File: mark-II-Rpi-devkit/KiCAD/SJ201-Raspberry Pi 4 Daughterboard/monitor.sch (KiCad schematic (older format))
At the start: 0 parts

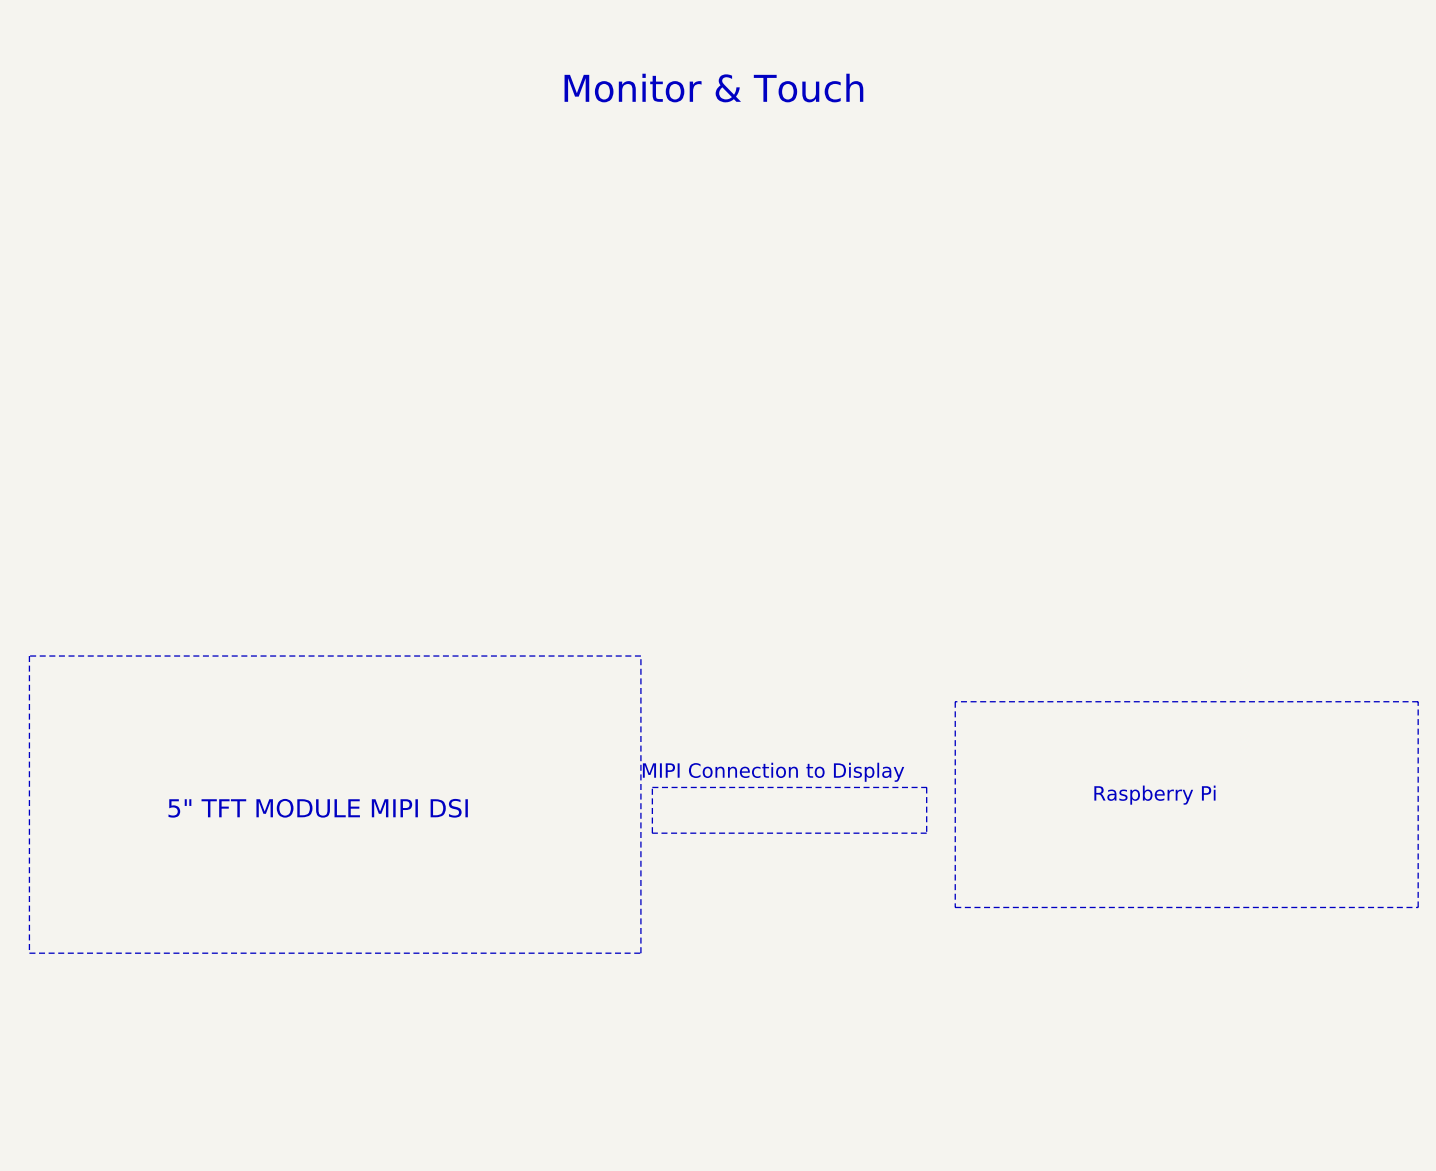
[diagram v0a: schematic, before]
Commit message: Rev4 Update - fix some wiring, export for printing Rev 4
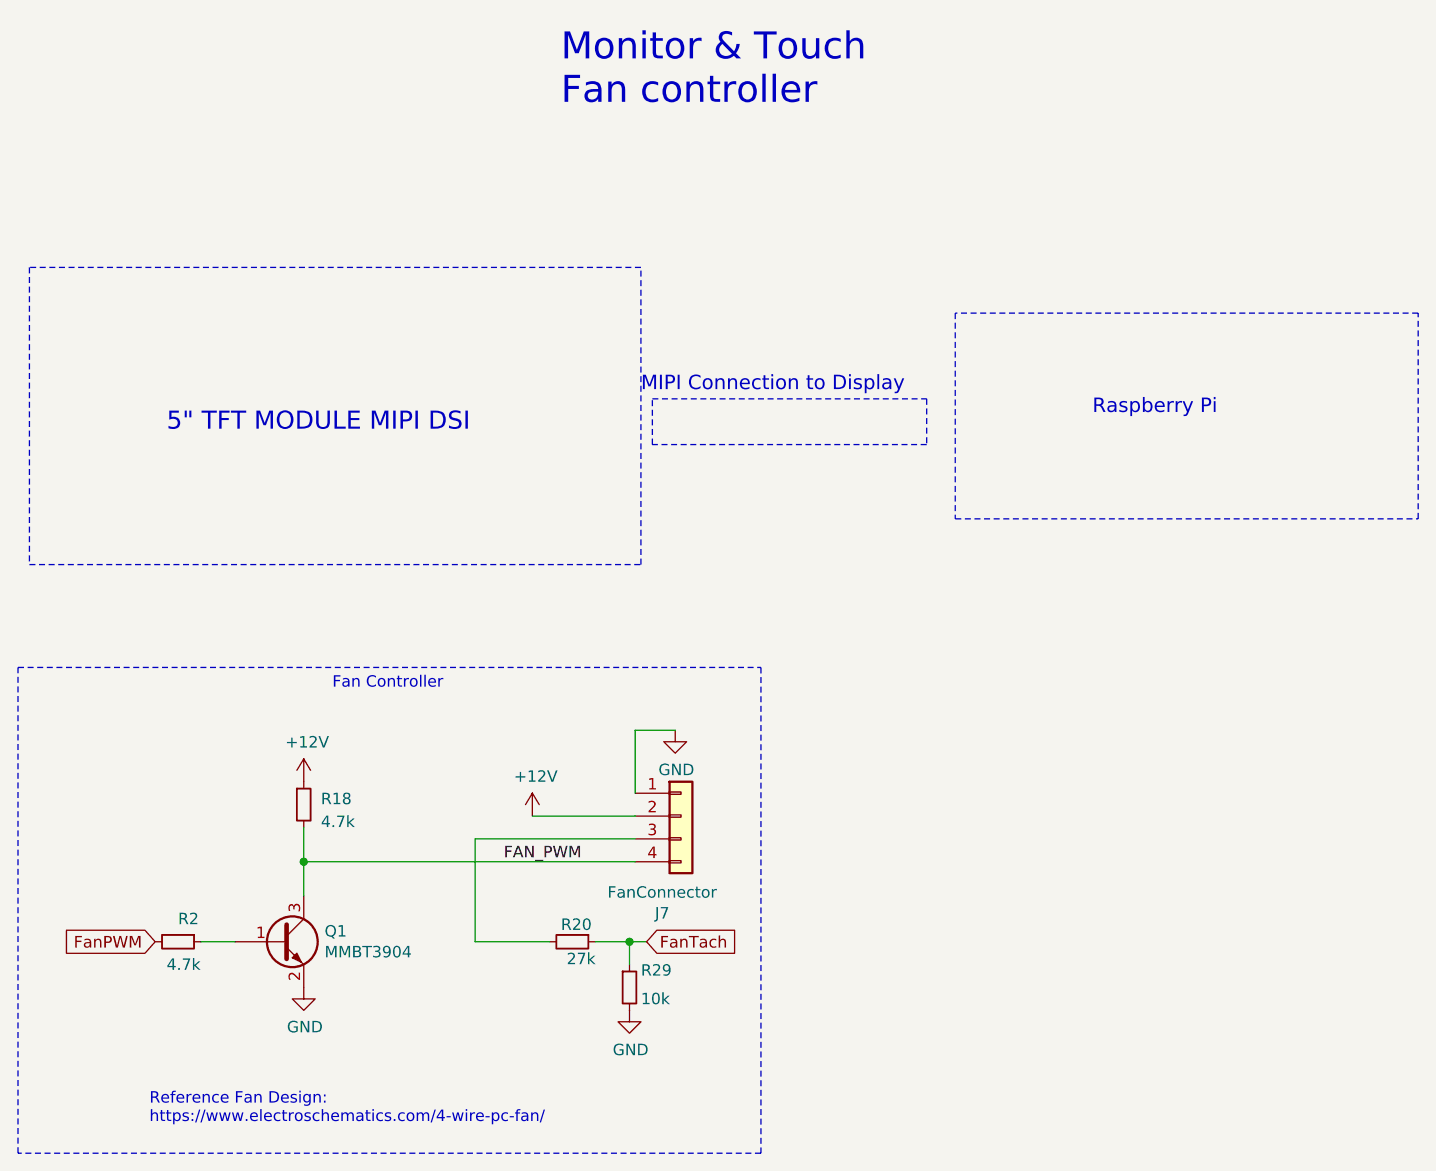
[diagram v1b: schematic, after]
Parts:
- added J7: FanConnector, Connector:FanPinHeader_1x04_P2.54mm_Vertical, symbol Connector_Generic:Conn_01x04
- added Q1: MMBT3904, Package_TO_SOT_SMD:SOT-23, symbol Transistor_BJT:MMBT3904
- added R18, R2: 4.7k, Resistor_SMD:R_0402_1005Metric, symbol Device:R_Small
- added R20: 27k, Resistor_SMD:R_0402_1005Metric, symbol Device:R_Small
- added R29: 10k, Resistor_SMD:R_0402_1005Metric, symbol Device:R_Small
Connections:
- new net: Q1.1 (B), R2.1
- new net: J7.3 (Pin_3), R20.2
- new net +12V: J7.2 (Pin_2), R18.1
- new net FAN_PWM: J7.4 (Pin_4), Q1.3 (C), R18.2
- new net FanPWM: R2.2
- new net FanTach: R20.1, R29.1
- new net GND: J7.1 (Pin_1), Q1.2 (E), R29.2
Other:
- note added: "Fan Controller"
- note added: "Monitor & Touch\nFan controller"
- note added: "Reference Fan Design:\nhttps://www.electroschematics.com/4-wire-pc-fan/"
- note removed: "Monitor & Touch"
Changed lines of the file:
@@
 Sheet 4 7
 Title ""
-Date "2020-11-18"
-Rev "rev4 - 0.01"
+Date "2020-11-22"
+Rev "Rev4 - 0.03"
 Comp "Mycroft"
-Comment1 "SJ201 r4.01"
+Comment1 "SJ-201-R4"
 Comment2 ""
 Comment3 ""
@@
 $EndDescr
 Text Notes 4725 875  0    118  ~ 0
-Monitor & Touch
-Text Notes 7050 3925 0    63   ~ 0
+Monitor & Touch\nFan controller
+Text Notes 7050 2225 0    63   ~ 0
 Raspberry Pi
-Text Notes 5075 3825 0    63   ~ 0
+Text Notes 5075 2125 0    63   ~ 0
 MIPI Connection to Display
 Wire Notes Line
-	5125 4050 5125 3850
-Wire Notes Line
-	6325 4050 5125 4050
-Wire Notes Line
-	6325 3850 6325 4050
-Wire Notes Line
-	5125 3850 6325 3850
-Wire Notes Line
-	8475 3475 6450 3475
-Wire Notes Line
-	8475 4375 8475 3475
-Wire Notes Line
-	6450 4375 8475 4375
-Wire Notes Line
-	6450 3475 6450 4375
-Text Notes 3000 4000 0    79   ~ 0
+	5125 2350 5125 2150
+Wire Notes Line
+	6325 2350 5125 2350
+Wire Notes Line
+	6325 2150 6325 2350
+Wire Notes Line
+	5125 2150 6325 2150
+Wire Notes Line
+	8475 1775 6450 1775
+Wire Notes Line
+	8475 2675 8475 1775
+Wire Notes Line
+	6450 2675 8475 2675
+Wire Notes Line
+	6450 1775 6450 2675
+Text Notes 3000 2300 0    79   ~ 0
 5" TFT MODULE MIPI DSI
 Wire Notes Line
-	5075 3275 2400 3275
-Wire Notes Line
-	5075 4575 5075 3275
-Wire Notes Line
-	2400 4575 5075 4575
-Wire Notes Line
-	2400 3275 2400 4575
+	5075 1575 2400 1575
+Wire Notes Line
+	5075 2875 5075 1575
+Wire Notes Line
+	2400 2875 5075 2875
+Wire Notes Line
+	2400 1575 2400 2875
+$Comp
+L Transistor_BJT:MMBT3904 Q1
+U 1 1 60970DB4
+P 3500 4525
+F 0 "Q1" H 3691 4571 50  0000 L CNN
+F 1 "MMBT3904" H 3691 4480 50  0000 L CNN
+F 2 "Package_TO_SOT_SMD:SOT-23" H 3700 4450 50  0001 L CIN
+F 3 "" H 3500 4525 50  0001 L CNN
+F 4 "C20526" H 3500 4525 50  0001 C CNN "LCSC"
+	1    3500 4525
+	1    0    0    -1
+$EndComp
+$Comp
+L power:GND #PWR0117
+U 1 1 60971565
+P 3600 4725
+F 0 "#PWR0117" H 3600 4475 50  0001 C CNN
+F 1 "GND" H 3605 4552 50  0000 C CNN
+F 2 "" H 3600 4725 50  0001 C CNN
+F 3 "" H 3600 4725 50  0001 C CNN
+	1    3600 4725
+	1    0    0    -1
+$EndComp
+$Comp
+L Device:R_Small R?
+U 1 1 609730D3
+P 3050 4525
+AR Path="/5EA9C461/609730D3" Ref="R?"  Part="1"
+AR Path="/5EA9C67D/609730D3" Ref="R?"  Part="1"
+AR Path="/5EA9C76D/609730D3" Ref="R?"  Part="1"
+AR Path="/5EAB86B0/609730D3" Ref="R2"  Part="1"
+F 0 "R2" V 2950 4525 50  0000 L CNN
+F 1 "4.7k" V 3150 4475 50  0000 L CNN
+F 2 "Resistor_SMD:R_0402_1005Metric" H 3050 4525 50  0001 C CNN
+F 3 "~" H 3050 4525 50  0001 C CNN
+F 4 "0402WGF4701TCE" H 3050 4525 50  0001 C CNN "MPN"
+F 5 "C25900" H 3050 4525 50  0001 C CNN "LCSC"
+F 6 "RC0402JR-074K7L" H 3050 4525 50  0001 C CNN "Tempo"
+	1    3050 4525
+	0    1    1    0
+$EndComp
+$Comp
+L Device:R_Small R?
+U 1 1 609732C2
+P 3600 3925
+AR Path="/5EA9C461/609732C2" Ref="R?"  Part="1"
+AR Path="/5EA9C67D/609732C2" Ref="R?"  Part="1"
+AR Path="/5EA9C76D/609732C2" Ref="R?"  Part="1"
+AR Path="/5EAB86B0/609732C2" Ref="R18"  Part="1"
+F 0 "R18" H 3675 3950 50  0000 L CNN
+F 1 "4.7k" H 3675 3850 50  0000 L CNN
+F 2 "Resistor_SMD:R_0402_1005Metric" H 3600 3925 50  0001 C CNN
+F 3 "~" H 3600 3925 50  0001 C CNN
+F 4 "0402WGF4701TCE" H 3600 3925 50  0001 C CNN "MPN"
+F 5 "C25900" H 3600 3925 50  0001 C CNN "LCSC"
+F 6 "RC0402JR-074K7L" H 3600 3925 50  0001 C CNN "Tempo"
+	1    3600 3925
+	1    0    0    -1
+$EndComp
+$Comp
+L power:+12V #PWR?
+U 1 1 6098392C
+P 4600 3975
+AR Path="/5EAAC9A5/6098392C" Ref="#PWR?"  Part="1"
+AR Path="/5EA9C461/6098392C" Ref="#PWR?"  Part="1"
+AR Path="/5EAB86B0/6098392C" Ref="#PWR0158"  Part="1"
+F 0 "#PWR0158" H 4600 3825 50  0001 C CNN
+F 1 "+12V" H 4615 4148 50  0000 C CNN
+F 2 "" H 4600 3975 50  0001 C CNN
+F 3 "" H 4600 3975 50  0001 C CNN
+	1    4600 3975
+	1    0    0    -1
+$EndComp
+Text GLabel 5100 4525 2    51   Input ~ 0
+FanTach
+Wire Wire Line
+	5050 3975 4600 3975
+$Comp
+L Connector_Generic:Conn_01x04 J?
+U 1 1 60983934
+P 5250 3975
+AR Path="/5EA9C461/60983934" Ref="J?"  Part="1"
+AR Path="/5EAB86B0/60983934" Ref="J7"  Part="1"
+F 0 "J7" H 5168 3550 50  0000 C CNN
+F 1 "FanConnector" H 5168 3641 50  0000 C CNN
+F 2 "Connector:FanPinHeader_1x04_P2.54mm_Vertical" H 5250 3975 50  0001 C CNN
+F 3 "~" H 5250 3975 50  0001 C CNN
+	1    5250 3975
+	1    0    0    -1
+$EndComp
+Text GLabel 2950 4525 0    51   Input ~ 0
+FanPWM
+$Comp
+L power:GND #PWR0159
+U 1 1 60984A3E
+P 5225 3600
+F 0 "#PWR0159" H 5225 3350 50  0001 C CNN
+F 1 "GND" H 5230 3427 50  0000 C CNN
+F 2 "" H 5225 3600 50  0001 C CNN
+F 3 "" H 5225 3600 50  0001 C CNN
+	1    5225 3600
+	1    0    0    -1
+$EndComp
+Wire Wire Line
+	5225 3600 5050 3600
+Wire Wire Line
+	5050 3600 5050 3875
+Wire Wire Line
+	5050 4175 3600 4175
+Wire Wire Line
+	3600 4175 3600 4325
+Text Label 4475 4175 0    50   ~ 0
+FAN_PWM
+$Comp
+L power:+12V #PWR?
+U 1 1 60985749
+P 3600 3825
+AR Path="/5EAAC9A5/60985749" Ref="#PWR?"  Part="1"
+AR Path="/5EA9C461/60985749" Ref="#PWR?"  Part="1"
+AR Path="/5EAB86B0/60985749" Ref="#PWR0188"  Part="1"
+F 0 "#PWR0188" H 3600 3675 50  0001 C CNN
+F 1 "+12V" H 3615 3998 50  0000 C CNN
+F 2 "" H 3600 3825 50  0001 C CNN
+F 3 "" H 3600 3825 50  0001 C CNN
+	1    3600 3825
+	1    0    0    -1
+$EndComp
+Wire Wire Line
+	3600 4025 3600 4175
+Connection ~ 3600 4175
+Wire Wire Line
+	3300 4525 3150 4525
+Wire Wire Line
+	5050 4075 4350 4075
+Wire Wire Line
+	4350 4075 4350 4525
+Wire Wire Line
+	4350 4525 4675 4525
+$Comp
+L Device:R_Small R?
+U 1 1 6098617E
+P 4775 4525
+AR Path="/5EA9C461/6098617E" Ref="R?"  Part="1"
+AR Path="/5EA9C67D/6098617E" Ref="R?"  Part="1"
+AR Path="/5EA9C76D/6098617E" Ref="R?"  Part="1"
+AR Path="/5EAB86B0/6098617E" Ref="R20"  Part="1"
+F 0 "R20" V 4700 4475 50  0000 L CNN
+F 1 "27k" V 4850 4500 50  0000 L CNN
+F 2 "Resistor_SMD:R_0402_1005Metric" H 4775 4525 50  0001 C CNN
+F 3 "~" H 4775 4525 50  0001 C CNN
+F 4 "C25771" H 4775 4525 50  0001 C CNN "LCSC"
+	1    4775 4525
+	0    1    1    0
+$EndComp
+$Comp
+L power:GND #PWR0189
+U 1 1 60986B27
+P 5025 4825
+F 0 "#PWR0189" H 5025 4575 50  0001 C CNN
+F 1 "GND" H 5030 4652 50  0000 C CNN
+F 2 "" H 5025 4825 50  0001 C CNN
+F 3 "" H 5025 4825 50  0001 C CNN
+	1    5025 4825
+	1    0    0    -1
+$EndComp
+$Comp
+L Device:R_Small R?
+U 1 1 60987E5F
+P 5025 4725
+AR Path="/5EA9C461/60987E5F" Ref="R?"  Part="1"
+AR Path="/5EA9C67D/60987E5F" Ref="R?"  Part="1"
+AR Path="/5EAAC9A5/60987E5F" Ref="R?"  Part="1"
+AR Path="/5EAB86B0/60987E5F" Ref="R29"  Part="1"
+F 0 "R29" H 5075 4800 50  0000 L CNN
+F 1 "10k" H 5075 4675 50  0000 L CNN
+F 2 "Resistor_SMD:R_0402_1005Metric" H 5025 4725 50  0001 C CNN
+F 3 "~" H 5025 4725 50  0001 C CNN
+F 4 "RC0402FR-0710KL" H 5025 4725 50  0001 C CNN "MPN"
+F 5 "C25744" H 5025 4725 50  0001 C CNN "LCSC"
+	1    5025 4725
+	1    0    0    -1
+$EndComp
+Wire Wire Line
+	5100 4525 5025 4525
+Text Notes 2925 5325 0    50   ~ 0
+Reference Fan Design:\nhttps://www.electroschematics.com/4-wire-pc-fan/
+Wire Wire Line
+	5025 4625 5025 4525
+Connection ~ 5025 4525
+Wire Wire Line
+	5025 4525 4875 4525
+Text Notes 3725 3425 0    50   ~ 0
+Fan Controller
+Wire Notes Line
+	5600 3325 5600 5450
+Wire Notes Line
+	5600 5450 2350 5450
+Wire Notes Line
+	2350 5450 2350 3325
+Wire Notes Line
+	2350 3325 5600 3325
 $EndSCHEMATC
